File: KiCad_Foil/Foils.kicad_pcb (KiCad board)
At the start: 2 copper layers, 200 x 40 mm, 7 parts, among them J1 Screw_Terminal_01x02

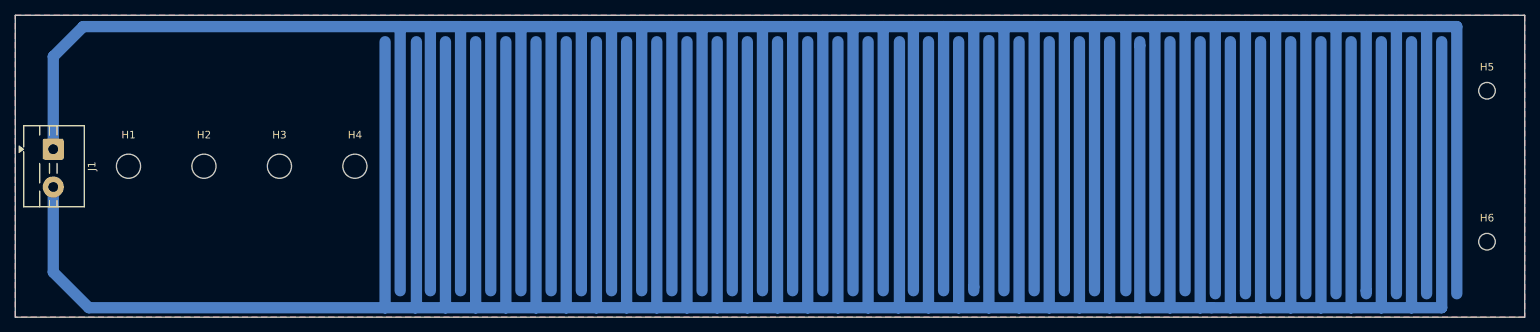
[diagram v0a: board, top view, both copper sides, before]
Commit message: New foils
New foils for better resistance measurement
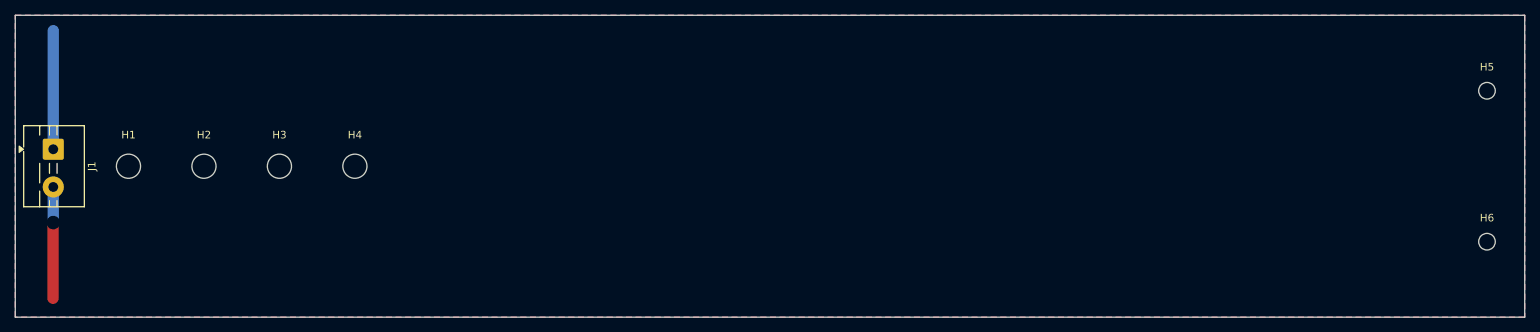
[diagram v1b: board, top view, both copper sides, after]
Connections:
- J1 pad 1: unconnected-(J1-Pin_1-Pad1) -> /NetA
- J1 pad 2: unconnected-(J1-Pin_2-Pad2) -> /NetB
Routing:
- net unconnected-(J1-Pin_2-Pad2): track 1466.4 -> 0.00 mm
- net unconnected-(J1-Pin_1-Pad1): track 1463.5 -> 0.00 mm
- net /NetA: track 0.00 -> 15.7 mm
- net /NetB: track 0.00 -> 14.8 mm, vias 0 -> 1
- added copper zone on B.Cu, net /NetA
- added copper zone on F.Cu, net /NetB
- removed copper zone on B.Cu, net (none)
- removed copper zone on F.Cu, net (none)
